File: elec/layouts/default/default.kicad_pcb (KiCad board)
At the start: 2 copper layers, 26 parts

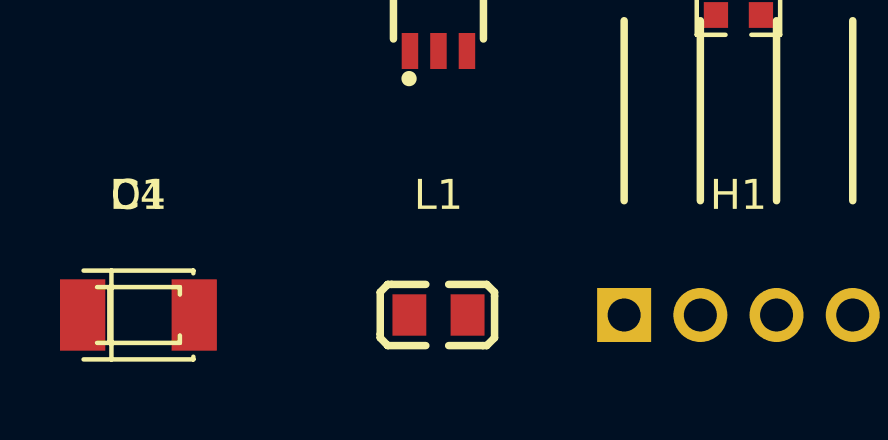
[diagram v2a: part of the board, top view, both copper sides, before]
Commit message: fix(buck): replace auto-selected inductor with explicit CENKER CKCS4018-4.7uH/M
The generic Inductor constraint caused Atopile to select FH CMP201209UD4R7KT
(C395016), a multilayer chip inductor rated at only 350mA — it would saturate
at 2× peak current (708mA). Replace with explicit CENKER CKCS4018-4.7uH/M
(C354574): Isat=1.7A, DCR=90mΩ, SMD 4018 package.
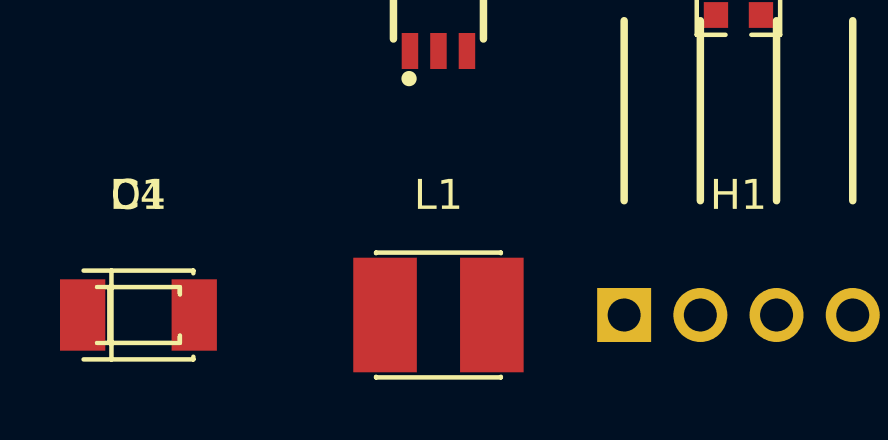
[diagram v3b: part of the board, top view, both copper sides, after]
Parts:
- L1: value 4.7µH ±10% -> (none); footprint FH_CMP201209UD4R7KT:L0805 -> CENKER_CKCS4018_4_7uH_M:IND-SMD_L4.0-W4.0_SWPA4018S
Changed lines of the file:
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@@
         )
     )
-    (footprint "FH_CMP201209UD4R7KT:L0805"
+    (footprint "CENKER_CKCS4018_4_7uH_M:IND-SMD_L4.0-W4.0_SWPA4018S"
         (layer "F.Cu")
         (at 10 0 0)
@@
             )
         )
-        (property "Value" "4.7µH ±10%"
+        (property "Value" ""
             (at 0 4 0)
             (layer "F.Fab")
@@
             )
         )
-        (property "checksum" "dc9384dc9a108805ad6f599f388ef05e64279bb50efc38e89b52fe18e5daa4d7"
+        (property "checksum" "84accde304dd7330a21d1540696496598563d874eb1cacd68fad7c062fb4e507"
             (at 0 0 0)
             (layer "User.9")
@@
             )
         )
-        (property "__atopile_lib_fp_hash__" "5261d4e1-955d-366a-039f-7adad5781138"
-            (at 0 0 0)
-            (layer "User.9")
-            (hide yes)
-            (effects
-                (font
-                    (size 0.125 0.125)
-                    (thickness 0.01875)
-                )
-            )
-        )
-        (property "LCSC" "C395016"
-            (at 0 0 0)
-            (layer "User.9")
-            (hide yes)
-            (effects
-                (font
-                    (size 0.125 0.125)
-                    (thickness 0.01875)
-                )
-            )
-        )
-        (property "Manufacturer" "FH(Guangdong Fenghua Advanced Tech)"
-            (at 0 0 0)
-            (layer "User.9")
-            (hide yes)
-            (effects
-                (font
-                    (size 0.125 0.125)
-                    (thickness 0.01875)
-                )
-            )
-        )
-        (property "Partnumber" "CMP201209UD4R7KT"
+        (property "__atopile_lib_fp_hash__" "3abe4cf1-ec25-6098-b89e-0d58b3066553"
+            (at 0 0 0)
+            (layer "User.9")
+            (hide yes)
+            (effects
+                (font
+                    (size 0.125 0.125)
+                    (thickness 0.01875)
+                )
+            )
+        )
+        (property "LCSC" "C354574"
+            (at 0 0 0)
+            (layer "User.9")
+            (hide yes)
+            (effects
+                (font
+                    (size 0.125 0.125)
+                    (thickness 0.01875)
+                )
+            )
+        )
+        (property "Manufacturer" "CENKER"
+            (at 0 0 0)
+            (layer "User.9")
+            (hide yes)
+            (effects
+                (font
+                    (size 0.125 0.125)
+                    (thickness 0.01875)
+                )
+            )
+        )
+        (property "Partnumber" "CKCS4018-4.7uH/M"
             (at 0 0 0)
             (layer "User.9")
@@
         (attr smd)
         (fp_line
-            (start -0.42 -1.02)
-            (end -1.56 -1.02)
-            (stroke
-                (width 0.25)
-                (type solid)
-            )
-            (layer "F.SilkS")
-        )
-        (fp_line
-            (start -1.56 -1.02)
-            (end -1.69 -1.02)
-            (stroke
-                (width 0.25)
-                (type solid)
-            )
-            (layer "F.SilkS")
-        )
-        (fp_line
-            (start -1.69 -1.02)
-            (end -1.94 -0.76)
-            (stroke
-                (width 0.25)
-                (type solid)
-            )
-            (layer "F.SilkS")
-        )
-        (fp_line
-            (start -1.94 -0.76)
-            (end -1.94 0.64)
-            (stroke
-                (width 0.25)
-                (type solid)
-            )
-            (layer "F.SilkS")
-        )
-        (fp_line
-            (start -1.94 0.64)
-            (end -1.94 0.76)
-            (stroke
-                (width 0.25)
-                (type solid)
-            )
-            (layer "F.SilkS")
-        )
-        (fp_line
-            (start -1.94 0.76)
-            (end -1.69 1.02)
-            (stroke
-                (width 0.25)
-                (type solid)
-            )
-            (layer "F.SilkS")
-        )
-        (fp_line
-            (start -1.69 1.02)
-            (end -0.42 1.02)
-            (stroke
-                (width 0.25)
-                (type solid)
-            )
-            (layer "F.SilkS")
-        )
-        (fp_line
-            (start 0.34 1.02)
-            (end 1.48 1.02)
-            (stroke
-                (width 0.25)
-                (type solid)
-            )
-            (layer "F.SilkS")
-        )
-        (fp_line
-            (start 1.48 1.02)
-            (end 1.61 1.02)
-            (stroke
-                (width 0.25)
-                (type solid)
-            )
-            (layer "F.SilkS")
-        )
-        (fp_line
-            (start 1.61 1.02)
-            (end 1.87 0.76)
-            (stroke
-                (width 0.25)
-                (type solid)
-            )
-            (layer "F.SilkS")
-        )
-        (fp_line
-            (start 1.87 0.76)
-            (end 1.87 -0.63)
-            (stroke
-                (width 0.25)
-                (type solid)
-            )
-            (layer "F.SilkS")
-        )
-        (fp_line
-            (start 1.87 -0.63)
-            (end 1.87 -0.76)
-            (stroke
-                (width 0.25)
-                (type solid)
-            )
-            (layer "F.SilkS")
-        )
-        (fp_line
-            (start 1.87 -0.76)
-            (end 1.61 -1.02)
-            (stroke
-                (width 0.25)
-                (type solid)
-            )
-            (layer "F.SilkS")
-        )
-        (fp_line
-            (start 1.61 -1.02)
-            (end 0.34 -1.02)
-            (stroke
-                (width 0.25)
+            (start -2.08 -2.06)
+            (end -2.08 -2.08)
+            (stroke
+                (width 0.15)
+                (type solid)
+            )
+            (layer "F.SilkS")
+        )
+        (fp_line
+            (start -2.08 -2.08)
+            (end 2.08 -2.08)
+            (stroke
+                (width 0.15)
+                (type solid)
+            )
+            (layer "F.SilkS")
+        )
+        (fp_line
+            (start 2.08 -2.08)
+            (end 2.08 -2.06)
+            (stroke
+                (width 0.15)
+                (type solid)
+            )
+            (layer "F.SilkS")
+        )
+        (fp_line
+            (start -2.08 2.06)
+            (end -2.08 2.08)
+            (stroke
+                (width 0.15)
+                (type solid)
+            )
+            (layer "F.SilkS")
+        )
+        (fp_line
+            (start -2.08 2.08)
+            (end 2.08 2.08)
+            (stroke
+                (width 0.15)
+                (type solid)
+            )
+            (layer "F.SilkS")
+        )
+        (fp_line
+            (start 2.08 2.08)
+            (end 2.08 2.06)
+            (stroke
+                (width 0.15)
                 (type solid)
             )
@@
         )
         (fp_circle
-            (center -1 0.64)
-            (end -0.97 0.64)
+            (center 2 1.97)
+            (end 2.03 1.97)
             (stroke
                 (width 0.06)
@@
         )
         (pad "1" smd rect
-            (at -0.97 0 0)
-            (size 1.13 1.38)
+            (at 1.78 0 0)
+            (size 2.12 3.82)
             (layers "F.Cu" "F.Paste" "F.Mask")
             (net 71 "SW")
         )
         (pad "2" smd rect
-            (at 0.97 0 0)
-            (size 1.13 1.38)
+            (at -1.78 0 0)
+            (size 2.12 3.82)
             (layers "F.Cu" "F.Paste" "F.Mask")
             (net 44 "esp32_vin")
         )
-        (model "${KIPRJMOD}/../../src/parts/FH_CMP201209UD4R7KT/R0805_L2.0-W1.3-H0.6.step"
+        (model "${KIPRJMOD}/../../src/parts/CENKER_CKCS4018_4_7uH_M/IND-SMD_L4.0-W4.0-H3.0.step"
             (offset
                 (xyz 0 0 0)
@@
             )
             (rotate
-                (xyz 0 0 0)
-            )
-        )
+                (xyz 0 0 270)
+            )
+        )

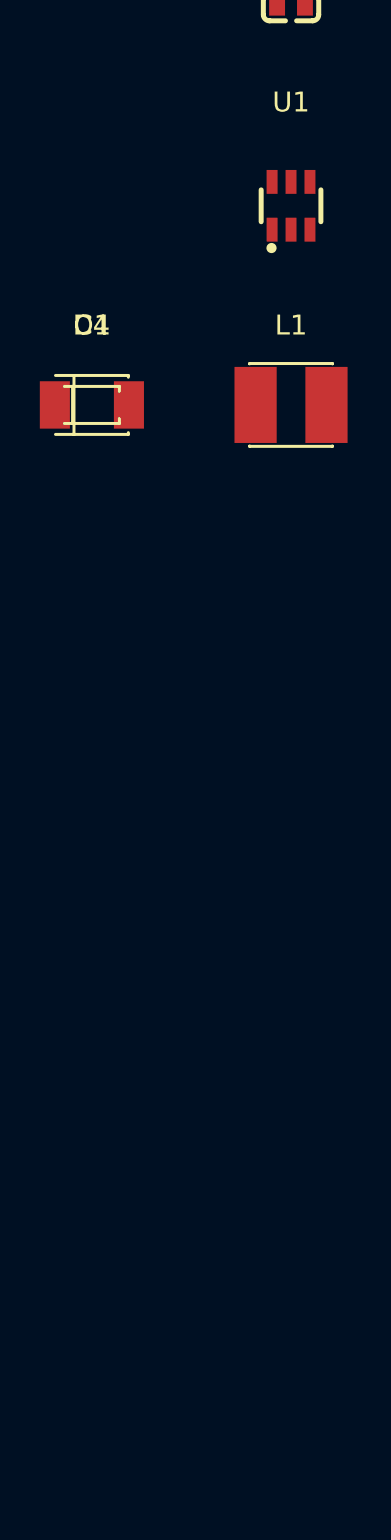
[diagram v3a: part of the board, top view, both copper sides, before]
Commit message: feat(headers): add ESP32-S3-DevKitC-1 female header interface
Hand-crafted 1×22 2.54mm KiCad footprint/symbol (no LCSC number needed —
snap from BOOMELE C9811 1×40P). ESP32Headers module wires all 44 pins:
GND, 3V3, 5V, GPIO4-10 connected; NC pins left unconnected. milsblo.ato
updated to use ESP32Headers; v3v3 now properly sourced through header.

ato build passes with correct footprint in netlist.
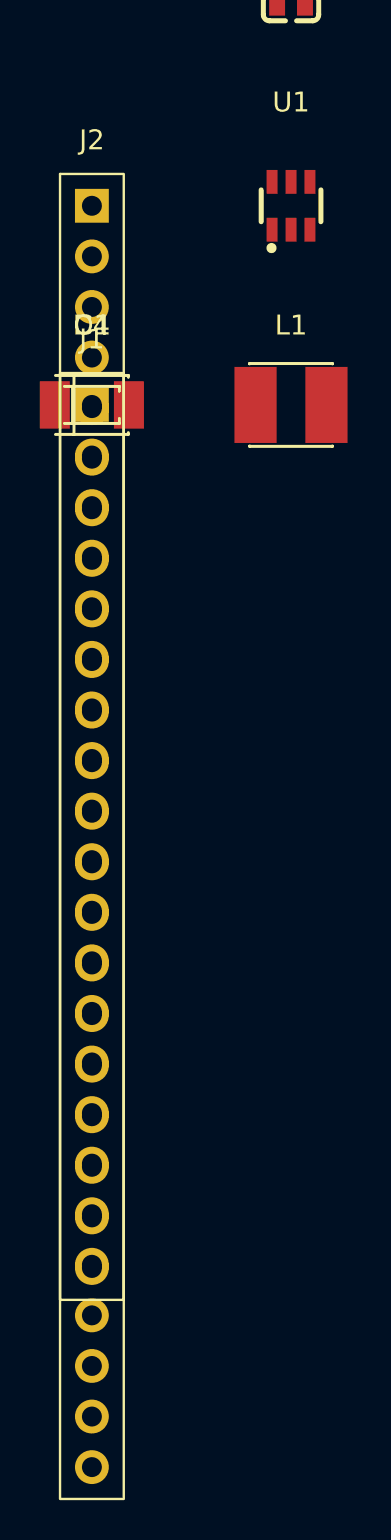
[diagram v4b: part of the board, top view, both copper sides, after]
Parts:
- added J1: , FemaleHeader_1x22_2v54mm:PinSocket_1x22_P2.54mm_Vertical, F.Cu at (0.00, 0.00)
- added J2: , FemaleHeader_1x22_2v54mm:PinSocket_1x22_P2.54mm_Vertical, F.Cu at (0.00, -10.0)
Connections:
- net esp32_vin renamed v5

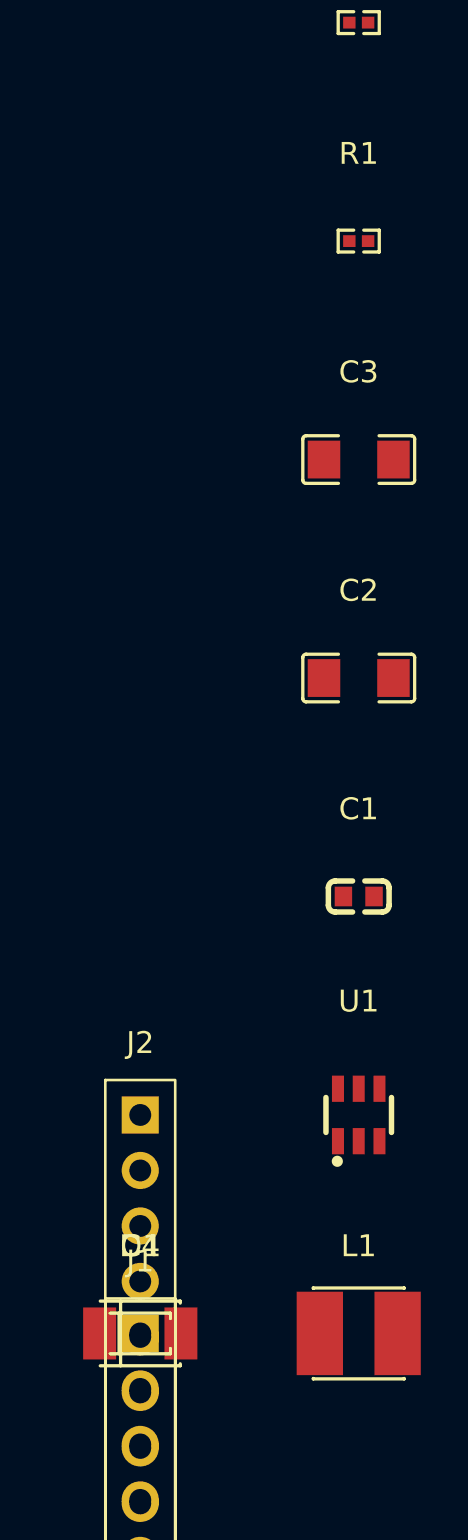
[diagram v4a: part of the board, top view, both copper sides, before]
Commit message: fix(review): pre-layout design review — voltage ratings, GPIO10, PG LED
Bugs fixed:
- Add max_voltage = 25V to 10000V on c_bulk (milsblo.ato) and c_in (buck_5v.ato)
  to prevent solver picking low-voltage parts (e.g. 6.3V AVX TAJB) on the 12V rail.
  Solver now picks KNSCHA RVT100UF35V167RV0082 (100µF 35V) for c_bulk.
- Disconnect GPIO10 from CH224K PG net: PG may be push-pull to VDD (5.1V), which
  exceeds ESP32 GPIO absolute maximum of 3.6V.
- Add c_vbus (100nF) in usb_pd.ato for local VBUS bypass during PD negotiation.

New: hardware PG LED indicator (replaces GPIO10 monitoring):
- Everlight 0603 green LED driven by Shikues MMBT3904 NPN transistor.
- NPN base: 100kΩ pullup to CH224K VDD + 10kΩ series from PG pin.
- LED lit when PG asserted; works for both open-drain and push-pull PG outputs.
- Remove GPIO10 binary_sensor from firmware/milsblo.yaml (now NC).

Docs: add 5V-only charger warning (board will not boot) and fan Pin 1 orientation
hazard note (bare header has no key tab — reversal puts 12V on GND pin).

ato build passes 22/22 parts.
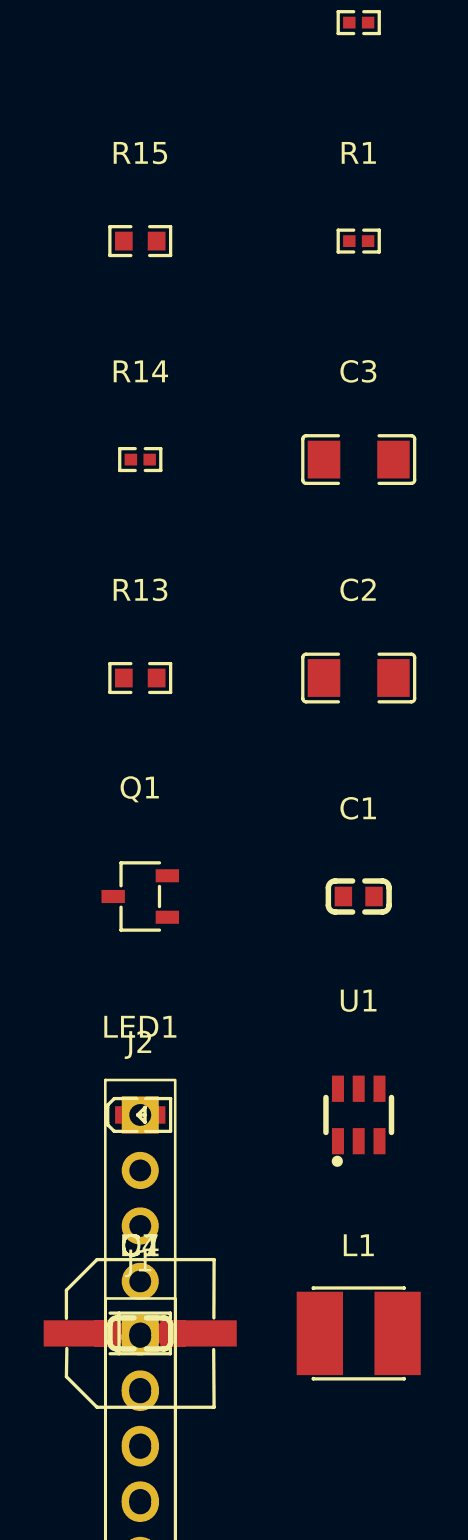
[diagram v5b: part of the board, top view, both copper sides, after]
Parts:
- added C7: 100nF ±10% 50V X7R, YAGEO_CC0603KRX7R9BB104:C0603, F.Cu at (0.00, 0.00)
- added LED1: , Everlight_Elec_19_217_GHC_YR1S2_3T:LED0603-RD, F.Cu at (0.00, -10.0)
- added Q1: , Shikues_MMBT3904:SOT-23-3_L2.9-W1.6-P1.90-LS2.8-BR, F.Cu at (0.00, -20.0)
- added R13: 470Ω ±1% 100mW, UNI_ROYAL_0603WAF4700T5E:R0603, F.Cu at (0.00, -30.0)
- added R14: 100kΩ ±1% 62.5mW, UNI_ROYAL_0402WGF1003TCE:R0402, F.Cu at (0.00, -40.0)
- added R15: 10kΩ ±1% 100mW, UNI_ROYAL_0603WAF1002T5E:R0603, F.Cu at (0.00, -50.0)
- C4: value 100µF ±10% -> 100µF ±20% 35V; footprint AVX_TAJB107K006RNJ:CASE-B_3528 -> KNSCHA_RVT100UF35V167RV0082:CAP-SMD_BD6.3-L6.6-W6.6-FD
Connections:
- net C renamed c_vdd-C
- J1 pad 16: pg -> gpio10
